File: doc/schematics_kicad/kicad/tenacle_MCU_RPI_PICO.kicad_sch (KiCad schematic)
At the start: 3 parts, among them T201 tentacle_octobus, T202 tentacle_relay

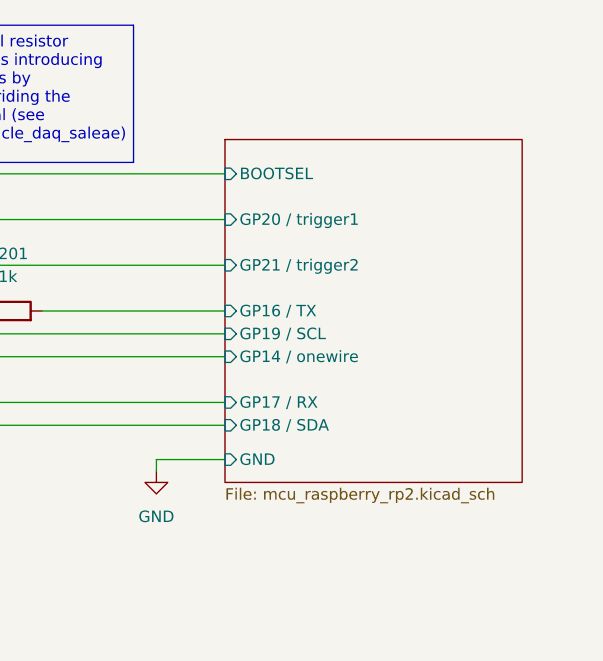
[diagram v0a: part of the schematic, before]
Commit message: MCU names as in micropython-git
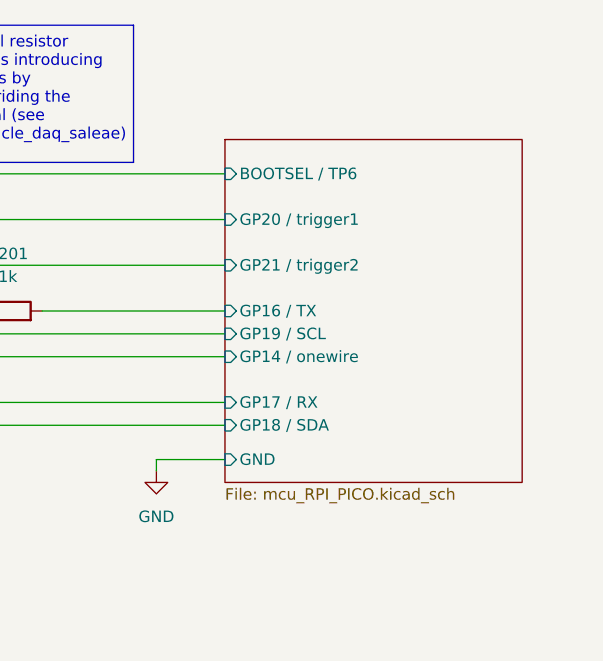
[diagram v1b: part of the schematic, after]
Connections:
- net MCU_RPI_PICO/BOOTSEL is gone; now on net SIGNAL_TRIGGER2: T202. (7b)
- new net MCU_RPI_PICO/BOOTSEL / TP6: T202. (7b)
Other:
- sheet raspberry rp3 renamed MCU_RPI_PICO
- sheet MCU_RPI_PICO: file mcu_raspberry_rp2.kicad_sch -> mcu_RPI_PICO.kicad_sch
- sheet MCU_RPI_PICO ports: added BOOTSEL / TP6; removed BOOTSEL
- title: tentacle_MCU_raspberry_pico -> tentacle_MCU_RPI_PICO
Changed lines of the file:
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@@
 	(paper "A4")
 	(title_block
-		(title "tentacle_MCU_raspberry_pico")
+		(title "tentacle_MCU_RPI_PICO")
 		(date "2024-07-16")
 		(company "Hans Märki, Märki Informatik")
@@
 			(color 0 0 0 0.0000)
 		)
-		(property "Sheetname" "raspberry rp3"
+		(property "Sheetname" "MCU_RPI_PICO"
 			(at 185.42 48.8184 0)
 			(effects
@@
 			)
 		)
-		(property "Sheetfile" "mcu_raspberry_rp2.kicad_sch"
+		(property "Sheetfile" "mcu_RPI_PICO.kicad_sch"
 			(at 185.42 88.2146 0)
 			(effects
@@
 			)
 		)
-		(pin "BOOTSEL" input
+		(pin "BOOTSEL {slash} TP6" input
 			(at 185.42 53.34 180)
 			(effects
